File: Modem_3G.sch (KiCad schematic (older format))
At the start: 30 parts, among them Con1 SIM8050-6-0-14-01-A, Q1 BC847B, U3 Full_M2M_Quad_SIM DNF

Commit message: Updated schematic
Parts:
- removed R14: 0R_0603, Resistor_Smd_0603:0R_0603, symbol Resistors_Smd0603:0R_0603
- R11, R12: value 10k_0402 -> 10k
- R13: value 100k_0402 -> 100k
- renumbered SP1 to Modem1
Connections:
- net labels added: 4V0, MODEM_POWER_IN, MODEM_PWR_GND, MODEM_PWR_ON, POWER_OUT_1V8, POWER_OUT_GND, UART_MODEM_1V8_RXD, UART_MODEM_1V8_TXD, USB_MODEM_D+, USB_MODEM_D-
- net labels removed: 3V8, CODEC_CLK, I2S_CLK, I2S_RXD, I2S_TXD, I2S_WA, LOCAL_MODEM_~W_DISABLE, LOCAL_USB_MODEM_D+, LOCAL_USB_MODEM_D-, MPCIE_SIM_CLK, MPCIE_SIM_DET, MPCIE_SIM_IO, MPCIE_SIM_RST, MPCIE_VSIM, NXP_I2C_1V8_SCL, NXP_I2C_1V8_SDA, POWER_1V8, POWER_3V8, UART_LOCAL_MODEM_1V8_RXD, UART_LOCAL_MODEM_1V8_TXD
- wire segments 122 -> 120
- no-connect marks 6 -> 11
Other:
- note removed: "2. SIM_DET pulled-up to recognize \nas SIM card present.\n\nSee: \nSARA-G3 and SARA-U2 series \nSystem Integration Manual\nUBLOX, March 2018\nRev. 27\npg. 44."
- note removed: "3. PWR_ON level must be properly fixed, \ne.g. adding a 100k pull-up to V_BCKP\n\nSee: \nSARA-G3 and SARA-U2 series \nSystem Integration Manual\nUBLOX, March 2018\nRev. 27\npg. 175."
- note removed: "Components C62, C42-C45, C46, C100-C103, Con1, D4-D7, R103 are fitted in variants: full, minipcie."
- note removed: "Components SP1, Ant1, C50, D8, L5, R16, R17, R18, R19, R20, R21, R38, Q2 are fitted in variant: full."
- note removed: "NOTE:\n-----------------\n1. UART crossed due\nto U270 pinout description"
- note removed: "Note 1."
- note removed: "Note 2."
- note removed: "Note 3."
- note removed: "To Mini-PCIe\nconnector"

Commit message: Added logic level shifter on pcb
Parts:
- removed U3: Full_M2M_Quad_SIM DNF, SIMchip:Full_M2M_Quad_SIM, symbol SIMchip:Full_M2M_Quad_SIM
- C23, C24, C25, C26: value 47pF_0402 -> 47pF/50V
- C27: value 220uF_6_3V_Polymer -> 220uF/6V3
- C28, C30, C31, C32: value 100nF_0603 -> 100nF/50V
- C29: value 47uF_1206 -> 47uF/6V3
- C33: value 10pF_0603 -> 10pF
- L4: value 39nH_0603 -> 39nH
- R10, R15: value 10k_0402 -> 10k
- R16: value 47k_0402 -> 47k
- R17: value 470R_0402 -> 470R
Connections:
- wire segments 120 -> 110
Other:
- note removed: "M2M"
- moved on the sheet: C27, C29, C30, C31

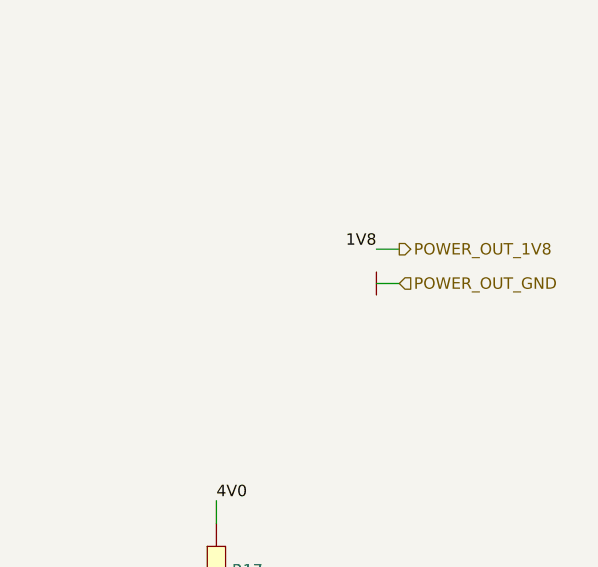
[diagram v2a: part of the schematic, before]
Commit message: Continue connections on schematic
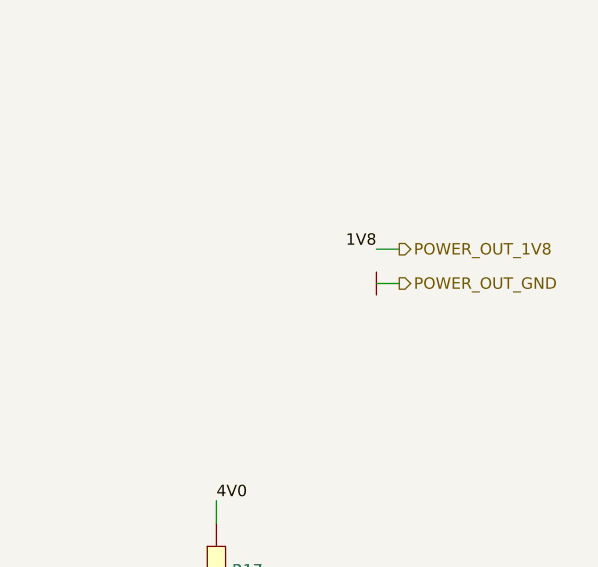
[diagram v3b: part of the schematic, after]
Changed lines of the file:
@@
 Wire Wire Line
 	14150 2200 14250 2200
-Text HLabel 14250 2350 2    50   Input ~ 0
+Text HLabel 14250 2350 2    50   Output ~ 0
 POWER_OUT_GND
 Wire Wire Line

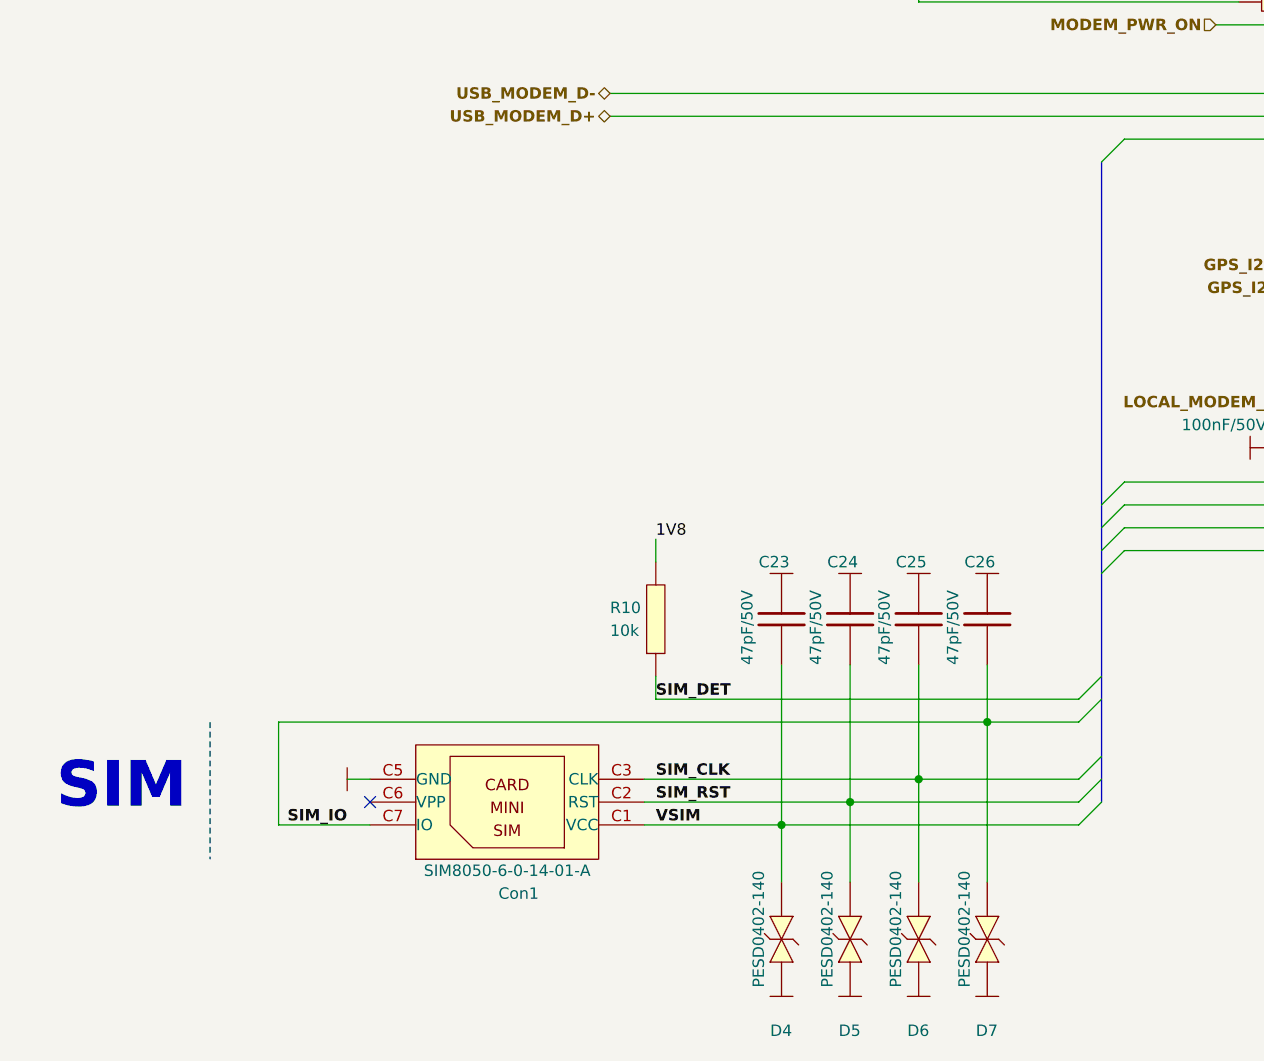
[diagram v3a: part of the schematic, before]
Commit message: Added connection for ethernet modules
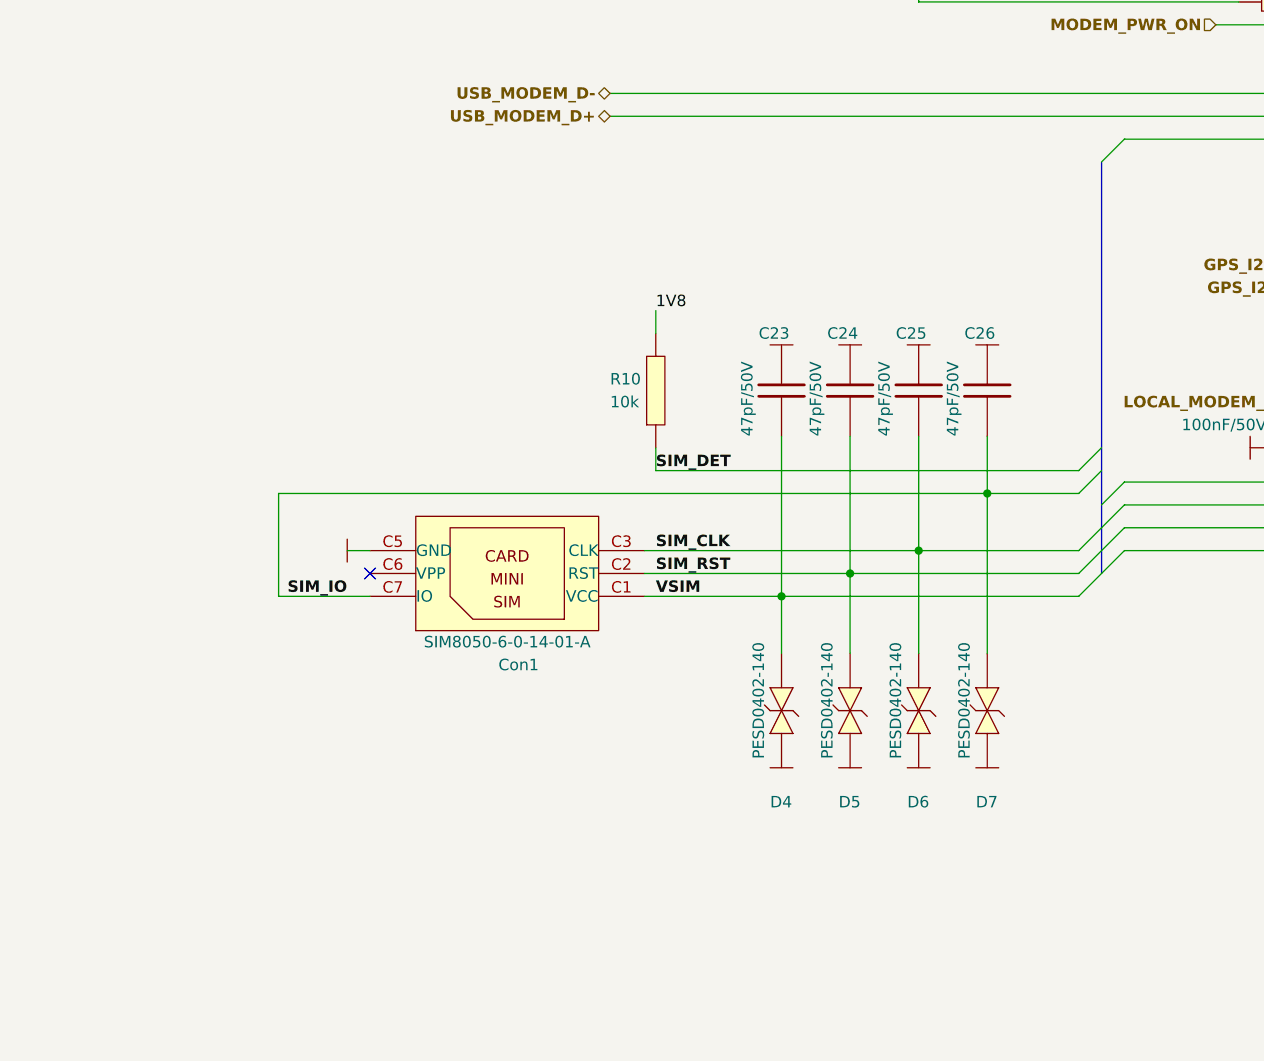
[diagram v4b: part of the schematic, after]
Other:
- note removed: "SIM"
- moved on the sheet: C23, C24, C25, C26, Con1, D4, D5, D6, D7, R10
